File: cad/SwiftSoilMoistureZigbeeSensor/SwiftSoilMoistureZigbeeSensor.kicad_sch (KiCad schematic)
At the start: 12 parts, among them J1 Probe, J2 BAT, J3 TagConnect, Q1 BSS84, SW1 Factory Reset, U1 TPS61221DCK, U2 E73-2G4M08S1C

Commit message: Footprint associations
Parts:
- C1, C2: footprint (none) -> Capacitor_SMD:C_0603_1608Metric
- D1: footprint (none) -> LED_SMD:LED_0201_0603Metric
- J1: footprint (none) -> Connector_PinHeader_1.27mm:PinHeader_1x03_P1.27mm_Horizontal
- J2: footprint (none) -> Connector_PinHeader_1.27mm:PinHeader_1x02_P1.27mm_Horizontal
- R1: footprint (none) -> Resistor_SMD:R_0201_0603Metric
- SW1: footprint (none) -> Button_Switch_SMD:SW_SPST_B3S-1000
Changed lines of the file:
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@@
       (effects (font (size 1.27 1.27)))
     )
-    (property "Footprint" "" (at 246.38 88.9 0)
+    (property "Footprint" "Connector_PinHeader_1.27mm:PinHeader_1x03_P1.27mm_Horizontal" (at 246.38 88.9 0)
       (effects (font (size 1.27 1.27)) hide)
     )
@@
       (effects (font (size 1.27 1.27)))
     )
-    (property "Footprint" "" (at 157.48 52.07 0)
+    (property "Footprint" "Connector_PinHeader_1.27mm:PinHeader_1x02_P1.27mm_Horizontal" (at 157.48 52.07 0)
       (effects (font (size 1.27 1.27)) hide)
     )
@@
       (effects (font (size 1.27 1.27)) (justify left))
     )
-    (property "Footprint" "" (at 209.2452 57.15 0)
+    (property "Footprint" "Capacitor_SMD:C_0603_1608Metric" (at 209.2452 57.15 0)
       (effects (font (size 1.27 1.27)) hide)
     )
@@
       (effects (font (size 1.27 1.27)) (justify left))
     )
-    (property "Footprint" "" (at 129.032 127 90)
+    (property "Footprint" "Resistor_SMD:R_0201_0603Metric" (at 129.032 127 90)
       (effects (font (size 1.27 1.27)) hide)
     )
@@
       (effects (font (size 1.27 1.27)) (justify right))
     )
-    (property "Footprint" "" (at 130.81 134.62 0)
+    (property "Footprint" "LED_SMD:LED_0201_0603Metric" (at 130.81 134.62 0)
       (effects (font (size 1.27 1.27)) hide)
     )
@@
       (effects (font (size 1.27 1.27)) (justify left))
     )
-    (property "Footprint" "" (at 172.4152 60.96 0)
+    (property "Footprint" "Capacitor_SMD:C_0603_1608Metric" (at 172.4152 60.96 0)
       (effects (font (size 1.27 1.27)) hide)
     )
@@
       (effects (font (size 1.27 1.27)) (justify left))
     )
-    (property "Footprint" "" (at 160.02 125.73 0)
-      (effects (font (size 1.27 1.27)) hide)
-    )
+    (property "Footprint" "Button_Switch_SMD:SW_SPST_B3S-1000" (at 160.02 125.73 0)
+      (effects (font (size 1.27 1.27)) hide)
+    )

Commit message: Routing
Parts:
- J1: footprint Connector_PinHeader_1.27mm:PinHeader_1x03_P1.27mm_Horizontal -> Connector_PinHeader_2.54mm:PinHeader_1x03_P2.54mm_Horizontal
- J2: footprint Connector_PinHeader_1.27mm:PinHeader_1x02_P1.27mm_Horizontal -> Connector_PinHeader_2.54mm:PinHeader_1x02_P2.54mm_Vertical
- L1: footprint (none) -> Inductor_SMD:L_Wuerth_MAPI-4020
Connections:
- net at U2.20 (P0.12): no longer SW1.1
- net at U2.35 (P0.24): now also SW1.1
- net at U2.36 (P1.00): no longer J3.6 (SWO)
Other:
- moved on the sheet: D1, R1, SW1

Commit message: CAD Stuff
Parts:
- removed J3: TagConnect, Connector:Tag-Connect_TC2030-IDC-NL_2x03_P1.27mm_Vertical, symbol Connector:Conn_ARM_SWD_TagConnect_TC2030-NL
- added J3: Conn_ARM_JTAG_SWD_10, Connector_PinHeader_1.27mm:PinHeader_2x05_P1.27mm_Vertical_SMD, symbol Connector:Conn_ARM_JTAG_SWD_10
- added JP1: Jumper_Prog, Connector_PinHeader_2.54mm:PinHeader_1x02_P2.54mm_Vertical, symbol Jumper:Jumper_2_Bridged
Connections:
- net +3.3V: now also J3.1 (VTref), JP1.2 (B); no longer C2.1, Q1.2 (S), U1.2 (FB), U1.4 (VOUT)
- net GND: now also J3.3 (GND), J3.5 (GND), J3.9 (GNDDetect)
- net at U2.26 (P0.18/RESET): now also J3.10 (~{RESET})
- net at U2.37 (SWDIO): now also J3.2 (SWDIO/TMS)
- net at U2.39 (SWDCLK): now also J3.4 (SWCLK/TCK)
- new net: C2.1, JP1.1 (A), Q1.2 (S), U1.2 (FB), U1.4 (VOUT)
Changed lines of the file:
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@@
   (junction (at 181.61 52.07) (diameter 0) (color 0 0 0 0)
   )
+  (junction (at 76.2 33.02) (diameter 0) (color 0 0 0 0)
+  )
+  (junction (at 171.45 52.07) (diameter 0) (color 0 0 0 0)
+  )
   (junction (at 227.33 49.53) (diameter 0) (color 0 0 0 0)
   )
-  (junction (at 76.2 33.02) (diameter 0) (color 0 0 0 0)
-  )
-  (junction (at 171.45 52.07) (diameter 0) (color 0 0 0 0)
-  )
   (junction (at 146.05 143.51) (diameter 0) (color 0 0 0 0)
   )
@@
   (junction (at 171.45 60.96) (diameter 0) (color 0 0 0 0)
   )
+  (junction (at 52.07 120.65) (diameter 0) (color 0 0 0 0)
+  )
   (junction (at 130.81 143.51) (diameter 0) (color 0 0 0 0)
   )
@@
   (junction (at 179.07 52.07) (diameter 0) (color 0 0 0 0)
   )
+  (junction (at 173.99 143.51) (diameter 0) (color 0 0 0 0)
+  )
+  (junction (at 191.77 60.96) (diameter 0) (color 0 0 0 0)
+  )
   (junction (at 227.33 33.02) (diameter 0) (color 0 0 0 0)
   )
-  (junction (at 173.99 143.51) (diameter 0) (color 0 0 0 0)
-  )
-  (junction (at 191.77 60.96) (diameter 0) (color 0 0 0 0)
+  (wire (pts (xy 52.07 120.65) (xy 49.53 120.65))
+    (stroke (width 0) (type default))
   )
   (wire (pts (xy 72.39 48.26) (xy 72.39 143.51))
@@
     (stroke (width 0) (type default))
   )
-  (wire (pts (xy 62.23 102.87) (xy 67.31 102.87))
+  (wire (pts (xy 64.77 102.87) (xy 67.31 102.87))
     (stroke (width 0) (type default))
   )
@@
     (stroke (width 0) (type default))
   )
-  (wire (pts (xy 227.33 33.02) (xy 227.33 49.53))
-    (stroke (width 0) (type default))
-  )
-  (wire (pts (xy 62.23 105.41) (xy 68.58 105.41))
+  (wire (pts (xy 64.77 105.41) (xy 68.58 105.41))
     (stroke (width 0) (type default))
   )
@@
     (stroke (width 0) (type default))
   )
-  (wire (pts (xy 52.07 113.03) (xy 52.07 143.51))
+  (wire (pts (xy 227.33 45.72) (xy 227.33 49.53))
+    (stroke (width 0) (type default))
+  )
+  (wire (pts (xy 227.33 33.02) (xy 227.33 35.56))
     (stroke (width 0) (type default))
   )
@@
     (stroke (width 0) (type default))
   )
+  (wire (pts (xy 52.07 120.65) (xy 52.07 143.51))
+    (stroke (width 0) (type default))
+  )
   (wire (pts (xy 171.45 49.53) (xy 171.45 52.07))
     (stroke (width 0) (type default))
@@
     (stroke (width 0) (type default))
   )
-  (wire (pts (xy 76.2 92.71) (xy 76.2 33.02))
+  (wire (pts (xy 76.2 90.17) (xy 76.2 33.02))
     (stroke (width 0) (type default))
   )
@@
     (stroke (width 0) (type default))
   )
-  (wire (pts (xy 52.07 92.71) (xy 76.2 92.71))
+  (wire (pts (xy 52.07 90.17) (xy 76.2 90.17))
     (stroke (width 0) (type default))
   )
@@
     (stroke (width 0) (type default))
   )
-  (wire (pts (xy 64.77 55.88) (xy 69.85 55.88))
+  (wire (pts (xy 69.85 55.88) (xy 64.77 55.88))
     (stroke (width 0) (type default))
   )
@@
     (stroke (width 0) (type default))
   )
-  (wire (pts (xy 62.23 97.79) (xy 69.85 97.79))
+  (wire (pts (xy 64.77 97.79) (xy 69.85 97.79))
     (stroke (width 0) (type default))
   )
@@
     )
   )
+  (symbol (lib_id "Jumper:Jumper_2_Bridged") (at 227.33 40.64 90) (unit 1)
+    (in_bom yes) (on_board yes) (dnp no) (fields_autoplaced)
+    (property "Reference" "JP1" (at 228.6 39.37 90)
+      (effects (font (size 1.27 1.27)) (justify right))
+    )
+    (property "Value" "Jumper_Prog" (at 228.6 41.91 90)
+      (effects (font (size 1.27 1.27)) (justify right))
+    )
+    (property "Footprint" "Connector_PinHeader_2.54mm:PinHeader_1x02_P2.54mm_Vertical" (at 227.33 40.64 0)
+      (effects (font (size 1.27 1.27)) hide)
+    )
+    (property "Datasheet" "~" (at 227.33 40.64 0)
+      (effects (font (size 1.27 1.27)) hide)
+    )
+    (pin "1")
+    (pin "2")
+    (instances
+      (project "SwiftSoilMoistureZigbeeSensor"
+        (path "/abcc6947-5804-4900-9240-6fa6b27c7542"
+          (reference "JP1") (unit 1)
+        )
+      )
+    )
+  )
+  (symbol (lib_id "Connector:Conn_ARM_JTAG_SWD_10") (at 52.07 105.41 0) (unit 1)
+    (in_bom yes) (on_board yes) (dnp no) (fields_autoplaced)
+    (property "Reference" "J3" (at 40.64 104.14 0)
+      (effects (font (size 1.27 1.27)) (justify right))
+    )
+    (property "Value" "Conn_ARM_JTAG_SWD_10" (at 40.64 106.68 0)
+      (effects (font (size 1.27 1.27)) (justify right))
+    )
+    (property "Footprint" "Connector_PinHeader_1.27mm:PinHeader_2x05_P1.27mm_Vertical_SMD" (at 52.07 105.41 0)
+      (effects (font (size 1.27 1.27)) hide)
+    )
+    (property "Datasheet" "http://infocenter.arm.com/help/topic/com.arm.doc.ddi0314h/DDI0314H_coresight_components_trm.pdf" (at 43.18 137.16 90)
+      (effects (font (size 1.27 1.27)) hide)
+    )
+    (pin "5")
+    (pin "2")
+    (pin "3")
+    (pin "4")
+    (pin "6")
+    (pin "10")
+    (pin "1")
+    (pin "7")
+    (pin "9")
+    (pin "8")
+    (instances
+      (project "SwiftSoilMoistureZigbeeSensor"
+        (path "/abcc6947-5804-4900-9240-6fa6b27c7542"
+          (reference "J3") (unit 1)
+        )
+      )
+    )
+  )
   (symbol (lib_id "power:+3.3V") (at 227.33 26.67 0) (unit 1)
     (in_bom yes) (on_board yes) (dnp no) (fields_autoplaced)
@@
         )
       )
-    )
-  )
-  (symbol (lib_id "Connector:Conn_ARM_SWD_TagConnect_TC2030-NL") (at 54.61 102.87 0) (unit 1)
-    (in_bom no) (on_board yes) (dnp no) (fields_autoplaced)
-    (property "Reference" "J3" (at 48.26 101.6 0)
-      (effects (font (size 1.27 1.27)) (justify right))
-    )
-    (property "Value" "TagConnect" (at 48.26 104.14 0)
-      (effects (font (size 1.27 1.27)) (justify right))
-    )
-    (property "Footprint" "Connector:Tag-Connect_TC2030-IDC-NL_2x03_P1.27mm_Vertical" (at 54.61 120.65 0)
-      (effects (font (size 1.27 1.27)) hide)
-    )
-    (property "Datasheet" "https://www.tag-connect.com/wp-content/uploads/bsk-pdf-manager/TC2030-CTX_1.pdf" (at 54.61 118.11 0)
-      (effects (font (size 1.27 1.27)) hide)
-    )
-    (pin "5")
-    (pin "3")
-    (pin "4")
-    (pin "6")
-    (pin "1")
-    (pin "2")
-    (instances
-      (project "SwiftSoilMoistureZigbeeSensor"
-        (path "/abcc6947-5804-4900-9240-6fa6b27c7542"
-          (reference "J3") (unit 1)
-        )
-      )

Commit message: LED and R1 sizes to 0603
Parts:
- D1: footprint LED_SMD:LED_0201_0603Metric -> LED_SMD:LED_0603_1608Metric
- R1: footprint Resistor_SMD:R_0201_0603Metric -> Resistor_SMD:R_0603_1608Metric
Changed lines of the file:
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@@
       (effects (font (size 1.27 1.27)) (justify left))
     )
-    (property "Footprint" "Resistor_SMD:R_0201_0603Metric" (at 172.212 127 90)
+    (property "Footprint" "Resistor_SMD:R_0603_1608Metric" (at 172.212 127 90)
       (effects (font (size 1.27 1.27)) hide)
     )
@@
       (effects (font (size 1.27 1.27)) (justify right))
     )
-    (property "Footprint" "LED_SMD:LED_0201_0603Metric" (at 173.99 134.62 0)
+    (property "Footprint" "LED_SMD:LED_0603_1608Metric" (at 173.99 134.62 0)
       (effects (font (size 1.27 1.27)) hide)
     )

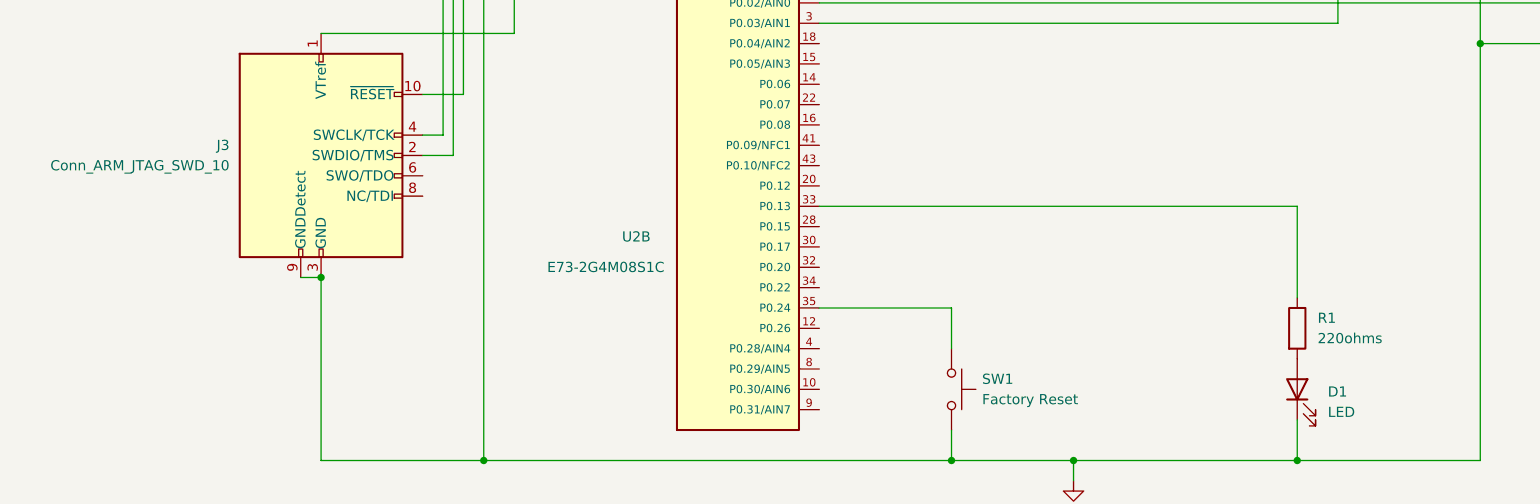
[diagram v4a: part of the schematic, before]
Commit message: Comp Label renaming
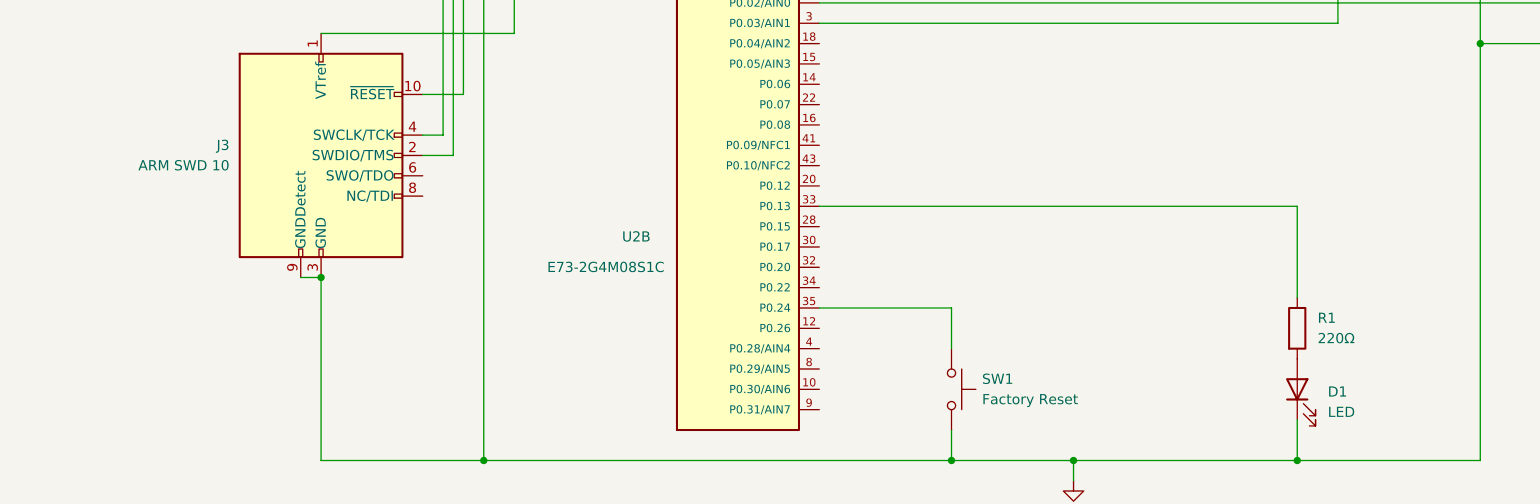
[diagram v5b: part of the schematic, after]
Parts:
- J3: value Conn_ARM_JTAG_SWD_10 -> ARM SWD 10
- R1: value 220ohms -> 220Ω
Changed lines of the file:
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@@
       (effects (font (size 1.27 1.27)) (justify right))
     )
-    (property "Value" "Conn_ARM_JTAG_SWD_10" (at 40.64 106.68 0)
+    (property "Value" "ARM SWD 10" (at 40.64 106.68 0)
       (effects (font (size 1.27 1.27)) (justify right))
     )
@@
       (effects (font (size 1.27 1.27)) (justify left))
     )
-    (property "Value" "220ohms" (at 176.53 128.27 0)
+    (property "Value" "220Ω" (at 176.53 128.27 0)
       (effects (font (size 1.27 1.27)) (justify left))
     )

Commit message: Added LCSC refs
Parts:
- C1, C2: LCSC (none) -> C329937
- D1: LCSC (none) -> C5246833
- J1: LCSC (none) -> C7089182
- J2: LCSC (none) -> C180247
- J3: LCSC (none) -> C2932107
- JP1: LCSC (none) -> C180247 + C3715628
- L1: LCSC (none) -> C87172
- Q1: LCSC (none) -> C493579
- R1: LCSC (none) -> C445820
- SW1: LCSC (none) -> C231324
- U1: LCSC (none) -> C2865756
- U2: Availability Not in stock -> (none); Check_prices https://www.snapeda.com/parts/E73-2G4M08S1C/EBYTE/view-part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 -> (none); LCSC (none) -> C356849; Price None -> (none); SnapEDA_Link https://www.snapeda.com/parts/E73-2G4M08S1C/EBYTE/view-part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 -> (none)
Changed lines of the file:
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@@
+      (effects (font (size 1.27 1.27)) hide)
+    )
+    (property "LCSC" " C7089182" (at 246.38 88.9 0)
       (effects (font (size 1.27 1.27)) hide)
     )
@@
       (effects (font (size 1.27 1.27)) hide)
     )
+    (property "LCSC" " C87172" (at 175.26 49.53 0)
+      (effects (font (size 1.27 1.27)) hide)
+    )
     (pin "2")
     (pin "1")
@@
     )
     (property "Datasheet" "~" (at 157.48 52.07 0)
+      (effects (font (size 1.27 1.27)) hide)
+    )
+    (property "LCSC" "C180247" (at 157.48 52.07 0)
       (effects (font (size 1.27 1.27)) hide)
     )
@@
       (effects (font (size 1.27 1.27)) (justify bottom) hide)
     )
-    (property "Price" "None" (at 46.99 50.8 0)
-      (effects (font (size 1.27 1.27)) (justify bottom) hide)
-    )
-    (property "SnapEDA_Link" "https://www.snapeda.com/parts/E73-2G4M08S1C/EBYTE/view-part/?ref=snap" (at 46.99 50.8 0)
-      (effects (font (size 1.27 1.27)) (justify bottom) hide)
-    )
     (property "MP" "E73-2G4M08S1C" (at 46.99 50.8 0)
       (effects (font (size 1.27 1.27)) (justify bottom) hide)
     )
-    (property "Availability" "Not in stock" (at 46.99 50.8 0)
-      (effects (font (size 1.27 1.27)) (justify bottom) hide)
-    )
-    (property "Check_prices" "https://www.snapeda.com/parts/E73-2G4M08S1C/EBYTE/view-part/?ref=eda" (at 46.99 50.8 0)
-      (effects (font (size 1.27 1.27)) (justify bottom) hide)
+    (property "LCSC" "C356849" (at 46.99 50.8 0)
+      (effects (font (size 1.27 1.27)) hide)
     )
     (pin "4")
@@
       (effects (font (size 1.27 1.27)) hide)
     )
+    (property "LCSC" "C329937" (at 208.28 53.34 0)
+      (effects (font (size 1.27 1.27)) hide)
+    )
     (pin "2")
     (pin "1")
@@
       (effects (font (size 1.27 1.27)) hide)
     )
+    (property "LCSC" "C180247 + C3715628" (at 227.33 40.64 0)
+      (effects (font (size 1.27 1.27)) hide)
+    )
     (pin "1")
     (pin "2")
@@
     )
     (property "Datasheet" "http://infocenter.arm.com/help/topic/com.arm.doc.ddi0314h/DDI0314H_coresight_components_trm.pdf" (at 43.18 137.16 90)
+      (effects (font (size 1.27 1.27)) hide)
+    )
+    (property "LCSC" "C2932107" (at 52.07 105.41 0)
       (effects (font (size 1.27 1.27)) hide)
     )
@@
       (effects (font (size 1.27 1.27)) hide)
     )
+    (property "LCSC" "C2865756" (at 191.77 52.07 0)
+      (effects (font (size 1.27 1.27)) hide)
+    )
     (pin "5")
     (pin "4")
@@
       (effects (font (size 1.27 1.27)) (justify bottom) hide)
     )
-    (property "Price" "None" (at 101.6 109.22 0)
-      (effects (font (size 1.27 1.27)) (justify bottom) hide)
-    )
-    (property "SnapEDA_Link" "https://www.snapeda.com/parts/E73-2G4M08S1C/EBYTE/view-part/?ref=snap" (at 101.6 109.22 0)
-      (effects (font (size 1.27 1.27)) (justify bottom) hide)
-    )
     (property "MP" "E73-2G4M08S1C" (at 101.6 109.22 0)
       (effects (font (size 1.27 1.27)) (justify bottom) hide)
     )
-    (property "Availability" "Not in stock" (at 101.6 109.22 0)
-      (effects (font (size 1.27 1.27)) (justify bottom) hide)
-    )
-    (property "Check_prices" "https://www.snapeda.com/parts/E73-2G4M08S1C/EBYTE/view-part/?ref=eda" (at 101.6 109.22 0)
-      (effects (font (size 1.27 1.27)) (justify bottom) hide)
+    (property "LCSC" "C356849" (at 101.6 109.22 0)
+      (effects (font (size 1.27 1.27)) hide)
     )
     (pin "4")
@@
       (effects (font (size 1.27 1.27)) hide)
     )
+    (property "LCSC" "C445820" (at 173.99 127 0)
+      (effects (font (size 1.27 1.27)) hide)
+    )
     (pin "1")
     (pin "2")
@@
       (effects (font (size 1.27 1.27)) (justify left) hide)
     )
+    (property "LCSC" "C493579" (at 224.79 72.39 0)
+      (effects (font (size 1.27 1.27)) hide)
+    )
     (pin "1")
     (pin "2")
@@
       (effects (font (size 1.27 1.27)) (justify bottom) hide)
     )
-    (property "Price" "None" (at 104.14 62.23 0)
-      (effects (font (size 1.27 1.27)) (justify bottom) hide)
-    )
-    (property "SnapEDA_Link" "https://www.snapeda.com/parts/E73-2G4M08S1C/EBYTE/view-part/?ref=snap" (at 104.14 62.23 0)
-      (effects (font (size 1.27 1.27)) (justify bottom) hide)
-    )
     (property "MP" "E73-2G4M08S1C" (at 104.14 62.23 0)
       (effects (font (size 1.27 1.27)) (justify bottom) hide)
     )
-    (property "Availability" "Not in stock" (at 104.14 62.23 0)
-      (effects (font (size 1.27 1.27)) (justify bottom) hide)
-    )
-    (property "Check_prices" "https://www.snapeda.com/parts/E73-2G4M08S1C/EBYTE/view-part/?ref=eda" (at 104.14 62.23 0)
-      (effects (font (size 1.27 1.27)) (justify bottom) hide)
+    (property "LCSC" "C356849" (at 104.14 62.23 0)
+      (effects (font (size 1.27 1.27)) hide)
     )
     (pin "4")
@@
       (effects (font (size 1.27 1.27)) hide)
     )
+    (property "LCSC" "C5246833" (at 173.99 134.62 0)
+      (effects (font (size 1.27 1.27)) hide)
+    )
     (pin "2")
     (pin "1")
@@
       (effects (font (size 1.27 1.27)) hide)
     )
+    (property "LCSC" "C329937" (at 171.45 57.15 0)
+      (effects (font (size 1.27 1.27)) hide)
+    )
     (pin "2")
     (pin "1")
@@
       (effects (font (size 1.27 1.27)) hide)
     )
+    (property "LCSC" "C231324" (at 130.81 134.62 0)
+      (effects (font (size 1.27 1.27)) hide)
+    )
